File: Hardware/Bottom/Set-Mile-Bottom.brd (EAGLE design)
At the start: 38 x 38 mm, 7 parts, among them U1 NRF52840_MDBT50

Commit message: updated board design to section 2
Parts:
- removed C1, C2: (no value), LinnesLab-Passives:C0603
- removed CORTEX2: CORTEX_DEBUG_PTH, LinnesLab-Connectors:2X5-PTH-1.27MM
- removed L1: 10u, LinnesLab-Passives:L0603
- removed SW2: (no value), LinnesLab-Switches:BUTTON-GULLWING
- removed XTAL1: 32.768kHz, LinnesLab-Clocks:2-SMD.NOLEAD.2.0MMTO1.2MM
- added C10, C11, C17, C18, C22, C24: 100n, LinnesLab-Passives:C0603
- added C14, C19: 2.2n, LinnesLab-Passives:C0603
- added C15, C16: 2.2u, LinnesLab-Passives:C0603
- added C20: 22u, LinnesLab-Passives:C0603
- added C21: 22n, LinnesLab-Passives:C0603
- added IMU1: LSM6DS3_CAST, LinnesLab-Sensors:LSM6DS3_CAST
- added J1: (no value), LinnesLab-Connectors:1X07
- added OP3: (no value), LinnesLab-AnalogIC:SO14
- added OP4: (no value), LinnesLab-AnalogIC:SOT23-5
- added Q1: (no value), LinnesLab-DiscreteSemi:SOT23-3
- added R13, R15, R19, R21: 220k, LinnesLab-Passives:R0603
- added R14, R22: 10M, LinnesLab-Passives:R0603
- added R16: (no value), LinnesLab-Passives:R0603
- added R17, R18: 10k, LinnesLab-Passives:R0402
- added R20, R23: 1M, LinnesLab-Passives:R0603
- added R24: 10k, LinnesLab-Passives:R0603
- added U$3: (no value), LinnesLab-Connectors:PPG.MODULE.2
- added U$4: AD5171, LinnesLab-DigitalIC:SOT-23-8
- U1: value NRF52840_MDBT50 -> AD5242-SO16; device LinnesLab-Microcontrollers:NRF52840_MDBT50 -> LinnesLab-DigitalIC:SO16
- moved U1 15.5 mm to (28.9, 10.9), turned to 270 degrees
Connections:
- net A3 renamed G.O2
- net D10 renamed G.A2
- removed net A0: U1.20
- removed net A1: U1.21
- removed net A2: U1.14
- removed net A4: U1.11
- removed net A5: U1.9
- removed net AREF: U1.12
- removed net D11: U1.22
- removed net D12: U1.24
- removed net D13: U1.26
- removed net D2: U1.54
- removed net D5: U1.25
- removed net D6: U1.23
- removed net D9: U1.19
- removed net DCCH: L1.2, U1.31
- removed net LED1: U1.8
- removed net LED2: U1.3
- removed net MISO: U1.39
- removed net MOSI: U1.37
- removed net N$3: C2.2, U1.17, XTAL1.P$2
- removed net NEOPIX: U1.38
- removed net QSPI_CS: U1.44
- removed net QSPI_DATA0: U1.41
- removed net QSPI_DATA1: U1.46
- removed net QSPI_DATA2: U1.45
- removed net QSPI_DATA3: U1.43
- removed net QSPI_SCK: U1.42
- removed net RESET: CORTEX2.10, SW2.3, U1.40
- removed net RXD: U1.48
- removed net SCK: U1.36
- removed net SWCLK: CORTEX2.4, U1.53
- removed net SWDIO: CORTEX2.2, U1.51
- removed net SWITCH: U1.50
- removed net SWO: CORTEX2.6, U1.47
- removed net TXD: U1.49
- removed net USBD+: U1.35
- removed net USBD-: U1.34
- removed net VDIV: U1.10
- removed net V_USB: U1.32
- new net A6/TIA: C10.2, C15.1, J1.7, OP4.1, U1.3
- new net A7/PPG: C21.2, J1.5, OP3.1, U1.14
- new net D29/LED.CTRL: J1.6, U$4.8
- new net G.A1: U1.2
- new net G.O1: U1.1
- new net G.W2: C21.1, OP3.2, R24.1, U1.15
- new net LED.C: Q1.3, U$3.LD1
- new net N$10: OP3.12, R17.1, R18.2
- new net N$13: C15.2, OP3.5, R13.1, R19.2
- new net N$15: C14.2, OP3.6, R14.1, R20.2
- new net N$16: C14.1, C16.1, OP3.7, R14.2
- new net N$17: C16.2, OP3.10, R15.1, R21.2
- new net N$18: C19.2, OP3.9, R22.1, R23.2
- new net N$19: C19.1, C20.1, OP3.8, R22.2
- new net N$20: C20.2, R24.2
- new net N$4: J1.4
- new net N$7: J1.1
- new net N$8: Q1.1, R16.2
- new net N$9: R16.1, U$4.1, U$4.7
- new net PD.C: C10.1, OP4.4, U$3.PD, U1.4
- new net VREF: OP3.13, OP3.14, OP3.3, R20.1, R23.1
- net 3.3V: now also C11.2, C17.2, C18.2, C22.2, C24.2, IMU1.2, OP3.4, OP4.5, R13.2, R15.2, R17.2, U$3.V+, U$4.2, U$4.6, U1.5, U1.6; no longer CORTEX2.1, L1.1, U1.28, U1.30
- net GND: now also C11.1, C17.1, C18.1, C22.1, C24.1, IMU1.1, OP3.11, OP4.2, OP4.3, Q1.2, R18.1, R19.1, R21.1, U$3.GND, U$4.3, U1.10, U1.11, U1.12, U1.9; no longer C1.2, C2.1, CORTEX2.3, CORTEX2.5, CORTEX2.7, CORTEX2.9, SW2.1, U1.1, U1.15, U1.2, U1.33, U1.55
- net N$5: now also J1.3; no longer C1.1, U1.18, XTAL1.P$1
- net N$6: now also J1.2; no longer CORTEX2.8
- net SCL: now also IMU1.3, U$4.4, U1.7; no longer U1.27
- net SDA: now also IMU1.4, U$4.5, U1.8; no longer U1.29
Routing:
- net VREF: track 0.00 -> 8.42 mm
- net N$10: track 0.00 -> 3.12 mm
- net GND: track 0.00 -> 1.37 mm, vias 0 -> 1
- added copper zone on layer 1, net 3.3V
- added copper zone on layer 16, net GND
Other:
- board size 38 x 38 mm -> 33 x 33 mm

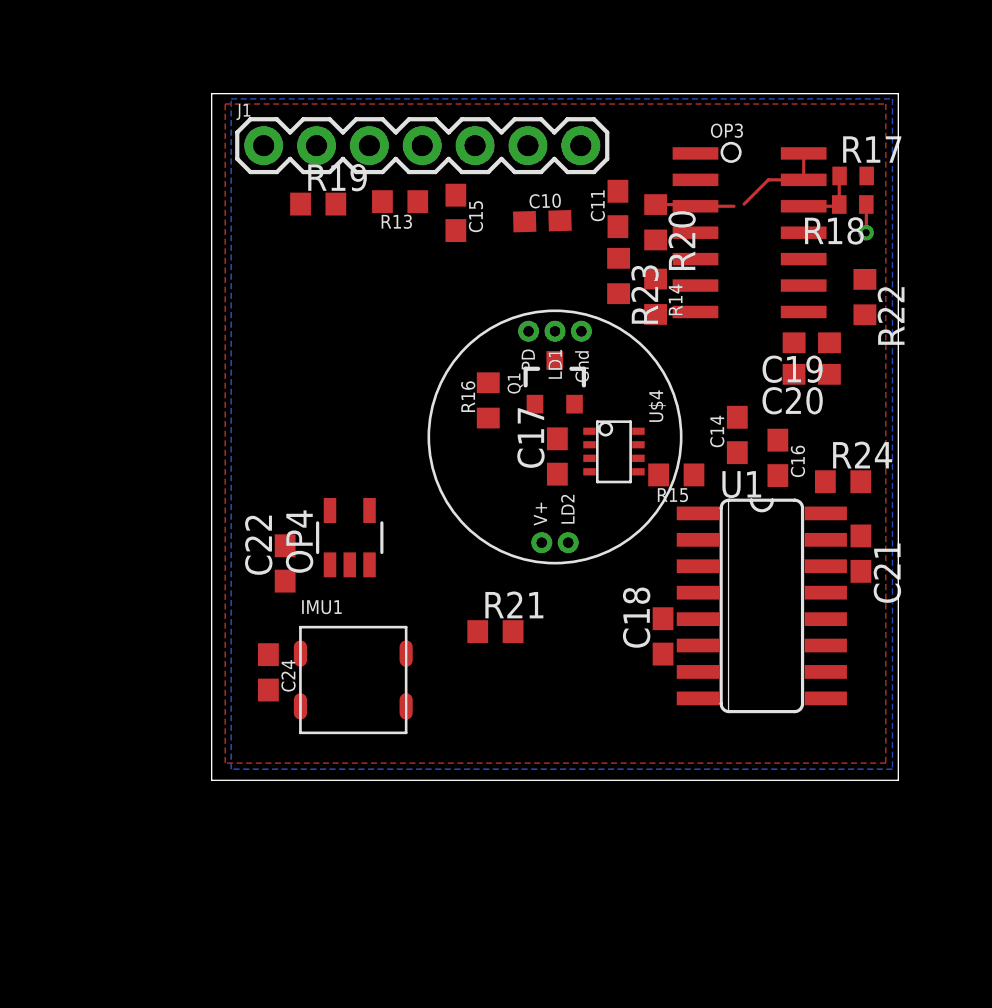
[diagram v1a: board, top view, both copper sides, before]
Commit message: routing bottom board and oranized top board
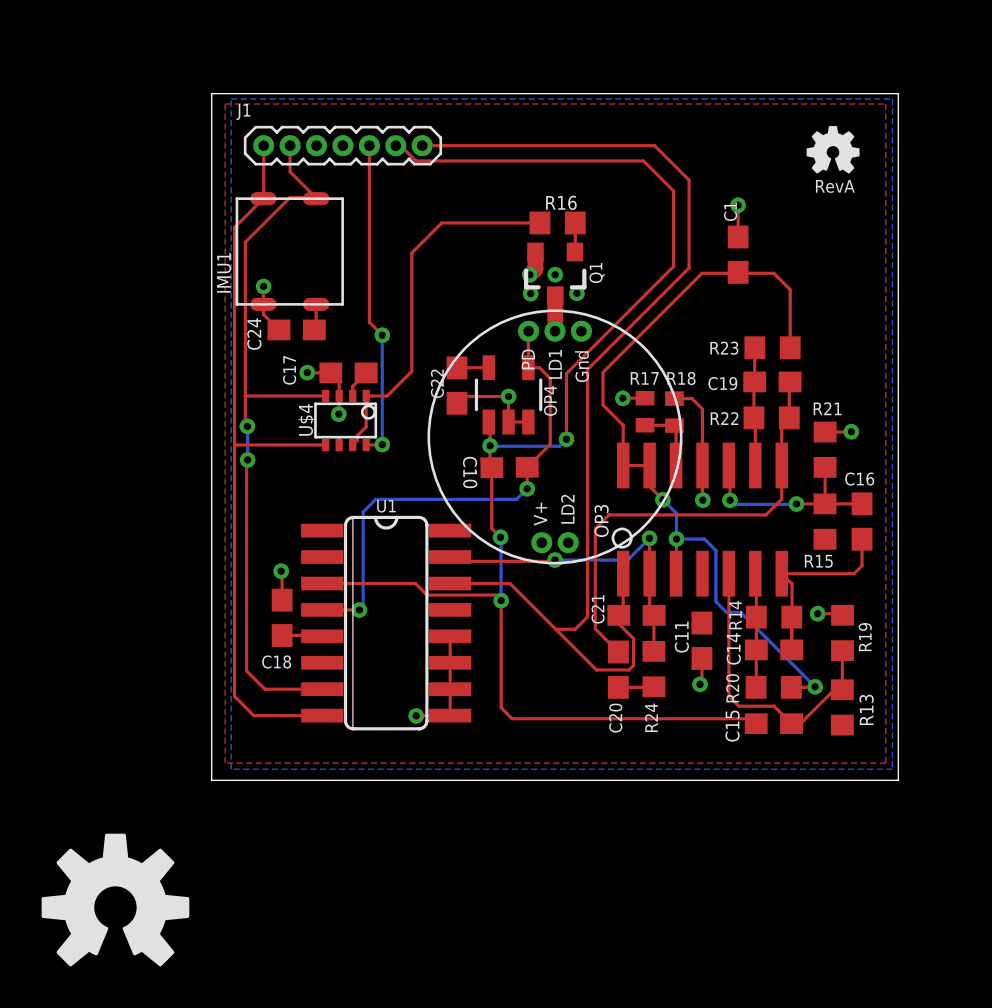
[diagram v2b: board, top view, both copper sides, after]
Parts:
- added C1: 100n, LinnesLab-Passives:C0603
- added LOGO1: REVISION.A, LinnesLab-Logos:REV.A
- added LOGO2: OSHW-LOGOL, LinnesLab-Logos:OSHW-LOGO-L
- added U$1: (no value), LinnesLab-Logos:OSHW-LOGO-MINI
- J1: device LinnesLab-Connectors:1X07 -> LinnesLab-Connectors:1X07_1.27MM
- moved R19 32.6 mm to (32.8, 9.58), turned to 270 degrees
- moved R13 32.3 mm to (32.8, 6.00), turned to 270 degrees
- moved C15 28.9 mm to (29.5, 5.22), turned to 0 degrees
- moved R20 23.1 mm to (29.5, 6.97), turned to 180 degrees
- moved C11 21.1 mm to (26.1, 9.20)
- moved IMU1 20.8 mm to (6.25, 27.9), turned to 90 degrees
- moved C18 18.3 mm to (5.89, 10.3), turned to 270 degrees
- moved R21 18.1 mm to (32.0, 18.4), turned to 270 degrees
- moved U1 18.1 mm to (10.9, 10.1)
- moved C20 17.0 mm to (22.0, 7.82), turned to 270 degrees
- moved C24 16.5 mm to (6.58, 24.1), turned to 0 degrees
- moved R14 16.4 mm to (29.5, 10.3), turned to 0 degrees
- moved R17 15.1 mm to (23.3, 20.2), turned to 90 degrees
- moved OP3 14.0 mm to (26.1, 15.0), turned to 0 degrees
- moved R18 13.2 mm to (24.7, 20.2), turned to 270 degrees
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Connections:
- removed net N$4: J1.4
- removed net N$5: J1.3
- removed net N$6: J1.2
- removed net N$7: J1.1
- net 3.3V: now also J1.4
- net A6/TIA: now also J1.6; no longer J1.7
- net A7/PPG: now also J1.7; no longer J1.5
- net D29/LED.CTRL: now also J1.5; no longer J1.6
- net GND: now also C1.1, J1.3
- net SCL: now also J1.2
- net SDA: now also J1.1
- net VREF: now also C1.2
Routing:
- net A6/TIA: track 0.00 -> 67.6 mm, vias 0 -> 4
- net A7/PPG: track 0.00 -> 53.7 mm
- net SDA: track 0.00 -> 36.0 mm
- net SCL: track 0.00 -> 35.9 mm, vias 0 -> 2
- net VREF: track 8.42 -> 38.2 mm, vias 0 -> 3
- net GND: track 1.37 -> 29.8 mm, vias 1 -> 15
- net PD.C: track 0.00 -> 23.7 mm, vias 0 -> 2
- net N$19: track 0.00 -> 21.7 mm
- net N$9: track 0.00 -> 17.7 mm
- net G.W2: track 0.00 -> 15.7 mm, vias 0 -> 2
- net D29/LED.CTRL: track 0.00 -> 15.4 mm, vias 0 -> 2
- net N$13: track 0.00 -> 14.4 mm
- net N$16: track 0.00 -> 10.7 mm
- net N$17: track 0.00 -> 9.90 mm, vias 0 -> 2
- net 3.3V: track 0.00 -> 7.55 mm, vias 0 -> 1
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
